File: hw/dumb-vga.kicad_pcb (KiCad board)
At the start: 2 copper layers, 62.2 x 83.8 mm, 26 parts, among them IC1 74HC590N, IC2 74HC590N, IC3 74HC590N, IC4 74HC574N, P1 CONN_01X02, P2 CONN_01X03, P3 CONN_01X03, U1 A29040C, X1 VGAF

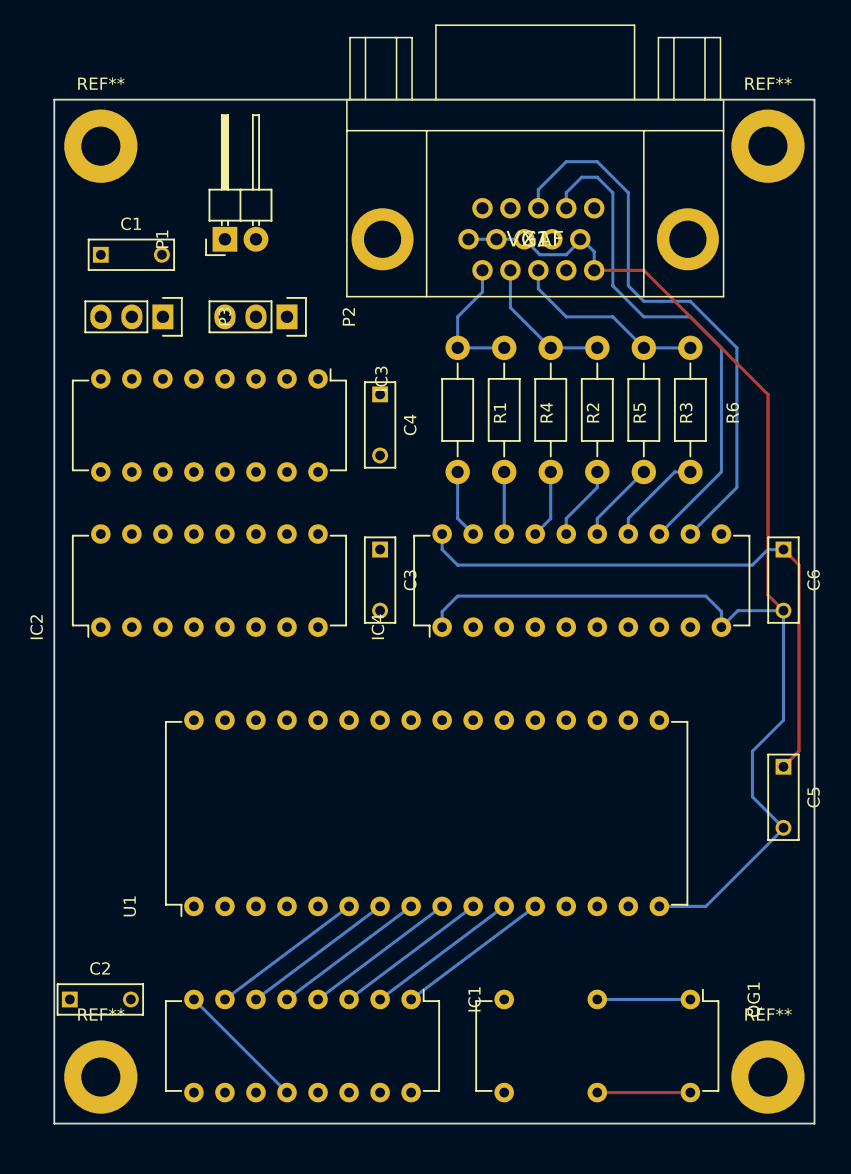
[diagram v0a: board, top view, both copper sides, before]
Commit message: Rearranged memory lines to make PCB layout easier, laid out more PCB.
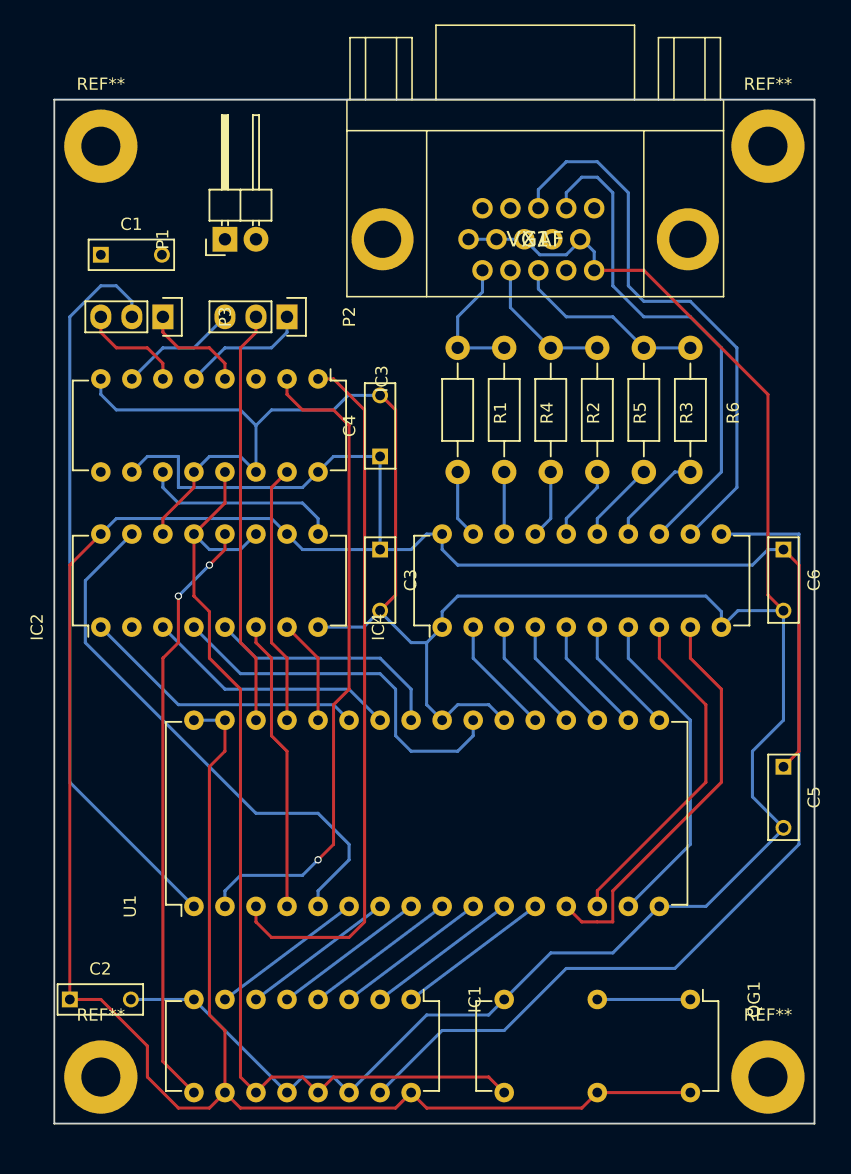
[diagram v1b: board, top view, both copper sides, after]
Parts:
- moved C4 5.08 mm to (130.8, 62.2), turned to 90 degrees
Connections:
- U1 pad 13: Net-(IC4-Pad2) -> Net-(IC4-Pad9)
- U1 pad 14: Net-(IC4-Pad3) -> Net-(IC4-Pad8)
- U1 pad 15: Net-(IC4-Pad4) -> Net-(IC4-Pad7)
- U1 pad 17: Net-(IC4-Pad5) -> Net-(IC4-Pad6)
- U1 pad 18: Net-(IC4-Pad6) -> Net-(IC4-Pad5)
- U1 pad 19: Net-(IC4-Pad7) -> Net-(IC4-Pad4)
- U1 pad 20: Net-(IC4-Pad8) -> Net-(IC4-Pad3)
- U1 pad 21: Net-(IC4-Pad9) -> Net-(IC4-Pad2)
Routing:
- net VCC: track 56.7 -> 243.0 mm
- net GND: track 125.6 -> 255.0 mm
- net Net-(IC1-Pad11): track 0.00 -> 82.5 mm
- net Net-(IC1-Pad15): track 0.00 -> 74.5 mm
- net Net-(P3-Pad2): track 0.00 -> 60.4 mm
- net Net-(IC3-Pad1): track 0.00 -> 58.0 mm
- net Net-(IC3-Pad2): track 0.00 -> 54.0 mm, vias 0 -> 1
- net Net-(IC1-Pad9): track 0.00 -> 48.9 mm, vias 0 -> 2
- net Net-(IC2-Pad15): track 0.00 -> 45.0 mm
- net Net-(P2-Pad2): track 0.00 -> 34.1 mm
- net Net-(IC4-Pad9): track 0.00 -> 33.2 mm
- net Net-(IC2-Pad4): track 0.00 -> 31.1 mm
- net Net-(IC4-Pad8): track 0.00 -> 28.1 mm
- net Net-(IC4-Pad7): track 0.00 -> 27.1 mm
- net Net-(IC2-Pad6): track 0.00 -> 23.9 mm
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
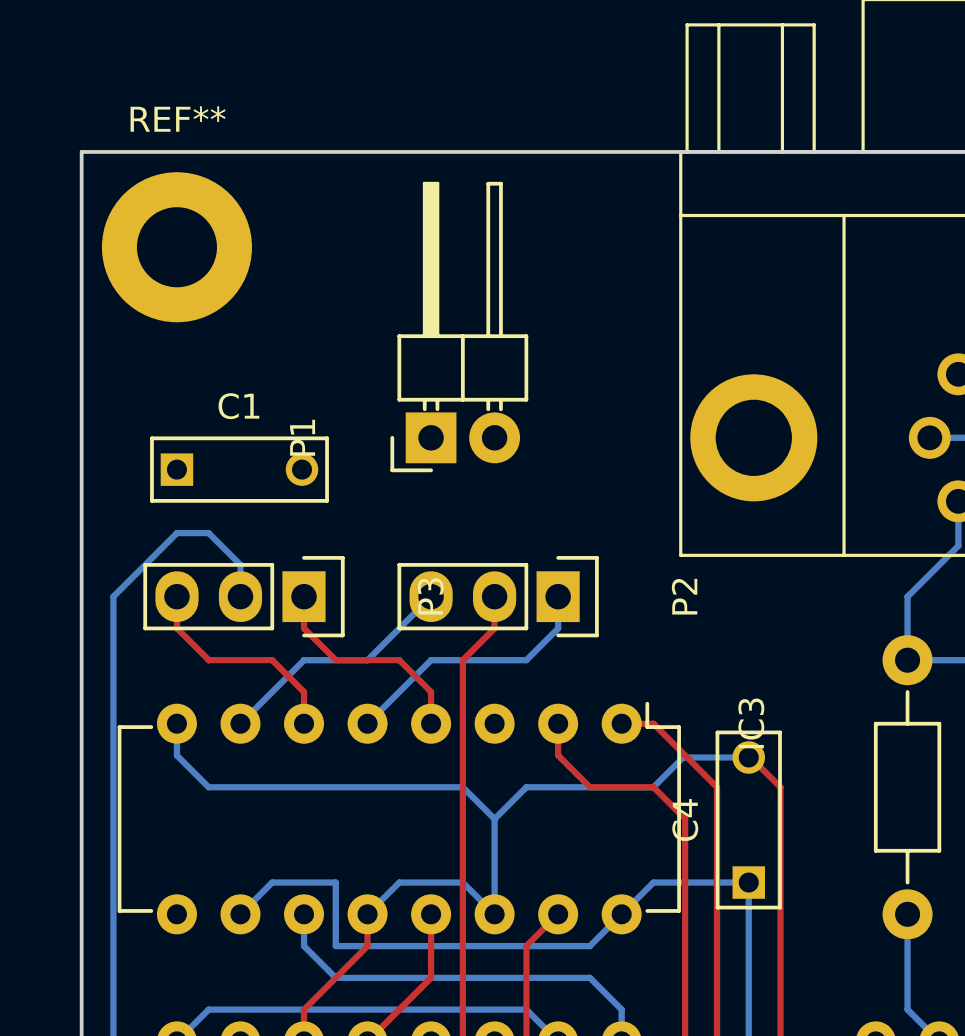
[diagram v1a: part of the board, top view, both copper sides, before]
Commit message: Changed power connector for something I have
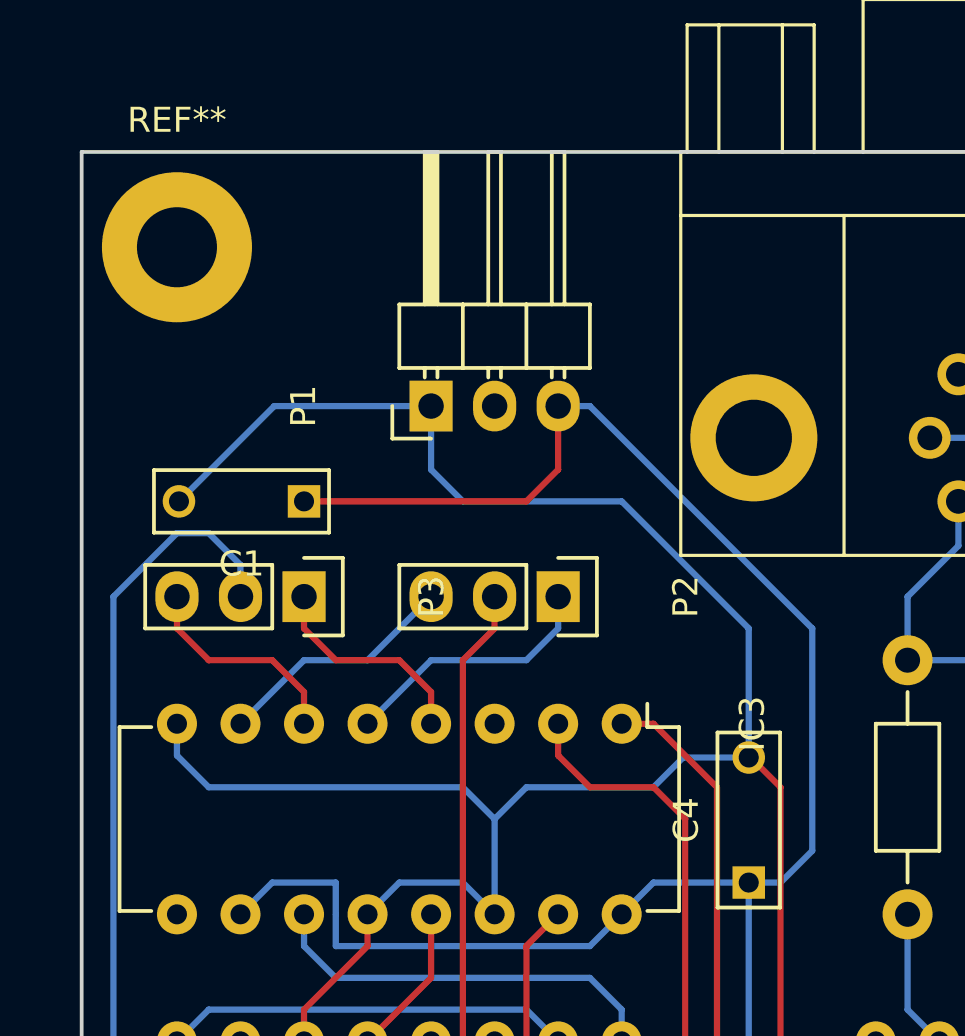
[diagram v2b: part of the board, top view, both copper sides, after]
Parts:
- P1: value CONN_01X02 -> CONN_01X03; footprint Pin_Headers:Pin_Header_Angled_1x02 -> Pin_Headers:Pin_Header_Angled_1x03
- moved C1 5.24 mm to (113.0, 47.0), turned to 180 degrees
- moved P1 1.27 mm to (118.1, 43.2)
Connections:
- P1 pad 2: VCC -> (no net)
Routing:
- net VCC: track 243.0 -> 282.0 mm
- net GND: track 255.0 -> 289.7 mm

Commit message: PCB tidy-up
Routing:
- added copper zone on B.Cu, net GND
- added copper zone on F.Cu, net GND
- added copper zone on F.Cu, net VCC
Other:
- net class Power added: clearance 0.2, trace_width 0.6, via_dia 0.6, via_drill 0.4

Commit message: Bumping schematic version number, labelling up PCB
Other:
- board text added: "dumb_vga - 2016 - v0.7"
- board text added: "sgf@arbitrary.name"
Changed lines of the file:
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@@
     (links 96)
     (no_connects 0)
-    (area 104.064999 32.944999 166.445001 116.915001)
+    (area 96.135475 26.663039 176.914525 119.085)
     (thickness 1.6)
-    (drawings 4)
+    (drawings 6)
     (tracks 333)
     (zones 0)
@@
   )
   (page A4)
+  (title_block
+    (title "Dumb VGA")
+    (rev v0.7)
+    (comment 1 "Simple circuit to generate VGA-like signal")
+  )
   (layers
-    (0 F.Cu signal hide)
+    (0 F.Cu signal)
     (31 B.Cu signal)
     (32 B.Adhes user)
@@
     (descr "14-lead dip package, row spacing 7.62 mm (300 mils)")
     (tags "dil dip 2.54 300")
-    (fp_text reference QG1 (at 0 -5.22 270) (layer F.SilkS)
+    (fp_text reference QG1 (at 3.81 7.62 360) (layer F.SilkS)
       (effects (font (size 1 1) (thickness 0.15)))
     )
@@
   (module Wire_Pads:SolderWirePad_single_2-5mmDrill (layer F.Cu)
     (at 162.56 113.03)
-    (fp_text reference REF** (at 0 -5.08) (layer F.SilkS)
+    (fp_text reference REF** (at 0 -5.08) (layer F.SilkS) hide
       (effects (font (size 1 1) (thickness 0.15)))
     )
@@
   (module Wire_Pads:SolderWirePad_single_2-5mmDrill (layer F.Cu)
     (at 107.95 113.03)
-    (fp_text reference REF** (at 0 -5.08) (layer F.SilkS)
+    (fp_text reference REF** (at 0 -5.08) (layer F.SilkS) hide
       (effects (font (size 1 1) (thickness 0.15)))
     )
@@
   (module Wire_Pads:SolderWirePad_single_2-5mmDrill (layer F.Cu)
     (at 107.95 36.83)
-    (fp_text reference REF** (at 0 -5.08) (layer F.SilkS)
+    (fp_text reference REF** (at 0 -5.08) (layer F.SilkS) hide
       (effects (font (size 1 1) (thickness 0.15)))
     )
@@
     (at 143.51 44.45)
     (attr virtual)
-    (fp_text reference X1 (at 0 0) (layer F.SilkS)
+    (fp_text reference X1 (at 0 0) (layer F.SilkS) hide
       (effects (font (thickness 0.15)))
     )
-    (fp_text value VGAF (at 0 0) (layer F.SilkS)
+    (fp_text value VGAF (at 0 0) (layer F.SilkS) hide
       (effects (font (thickness 0.15)))
     )
@@
     (descr "Film Capacitor Length 7mm x Width 2.5mm, Pitch 5mm")
     (tags Capacitor)
-    (fp_text reference C1 (at 2.5 -2.5 180) (layer F.SilkS)
+    (fp_text reference C1 (at 2.5 0 180) (layer F.SilkS)
       (effects (font (size 1 1) (thickness 0.15)))
     )
@@
     (descr "16-lead dip package, row spacing 7.62 mm (300 mils)")
     (tags "dil dip 2.54 300")
-    (fp_text reference IC1 (at 0 -5.22 270) (layer F.SilkS)
+    (fp_text reference IC1 (at 3.81 8.89 360) (layer F.SilkS)
       (effects (font (size 1 1) (thickness 0.15)))
     )
@@
     (descr "16-lead dip package, row spacing 7.62 mm (300 mils)")
     (tags "dil dip 2.54 300")
-    (fp_text reference IC2 (at 0 -5.22 90) (layer F.SilkS)
+    (fp_text reference IC2 (at 3.81 8.89 180) (layer F.SilkS)
       (effects (font (size 1 1) (thickness 0.15)))
     )
@@
     (descr "16-lead dip package, row spacing 7.62 mm (300 mils)")
     (tags "dil dip 2.54 300")
-    (fp_text reference IC3 (at 0 -5.22 270) (layer F.SilkS)
+    (fp_text reference IC3 (at 3.81 8.89 360) (layer F.SilkS)
       (effects (font (size 1 1) (thickness 0.15)))
     )
@@
     (descr "20-lead dip package, row spacing 7.62 mm (300 mils)")
     (tags "dil dip 2.54 300")
-    (fp_text reference IC4 (at 0 -5.22 90) (layer F.SilkS)
+    (fp_text reference IC4 (at 3.81 11.43 180) (layer F.SilkS)
       (effects (font (size 1 1) (thickness 0.15)))
     )
@@
     (descr "Resistor, Axial,  RM 10mm, 1/3W,")
     (tags "Resistor, Axial, RM 10mm, 1/3W,")
-    (fp_text reference R1 (at 0.24892 -3.50012 270) (layer F.SilkS)
+    (fp_text reference R1 (at 0.24892 0 270) (layer F.SilkS)
       (effects (font (size 1 1) (thickness 0.15)))
     )
@@
     (descr "Resistor, Axial,  RM 10mm, 1/3W,")
     (tags "Resistor, Axial, RM 10mm, 1/3W,")
-    (fp_text reference R2 (at 0.24892 -3.50012 270) (layer F.SilkS)
+    (fp_text reference R2 (at 0.24892 0 270) (layer F.SilkS)
       (effects (font (size 1 1) (thickness 0.15)))
     )
@@
     (descr "Resistor, Axial,  RM 10mm, 1/3W,")
     (tags "Resistor, Axial, RM 10mm, 1/3W,")
-    (fp_text reference R3 (at 0.24892 -3.50012 270) (layer F.SilkS)
+    (fp_text reference R3 (at 0.24892 0 270) (layer F.SilkS)
       (effects (font (size 1 1) (thickness 0.15)))
     )
@@
     (descr "Resistor, Axial,  RM 10mm, 1/3W,")
     (tags "Resistor, Axial, RM 10mm, 1/3W,")
-    (fp_text reference R4 (at 0.24892 -3.50012 270) (layer F.SilkS)
+    (fp_text reference R4 (at 0.24892 0 270) (layer F.SilkS)
       (effects (font (size 1 1) (thickness 0.15)))
     )
@@
     (descr "Resistor, Axial,  RM 10mm, 1/3W,")
     (tags "Resistor, Axial, RM 10mm, 1/3W,")
-    (fp_text reference R5 (at 0.24892 -3.50012 270) (layer F.SilkS)
+    (fp_text reference R5 (at 0.24892 0 270) (layer F.SilkS)
       (effects (font (size 1 1) (thickness 0.15)))
     )
@@
     (descr "Resistor, Axial,  RM 10mm, 1/3W,")
     (tags "Resistor, Axial, RM 10mm, 1/3W,")
-    (fp_text reference R6 (at 0.24892 -3.50012 270) (layer F.SilkS)
+    (fp_text reference R6 (at 0.24892 0 270) (layer F.SilkS)
       (effects (font (size 1 1) (thickness 0.15)))
     )
@@
     (descr "32-lead dip package, row spacing 15.24 mm (600 mils)")
     (tags "dil dip 2.54 600")
-    (fp_text reference U1 (at 0 -5.22 90) (layer F.SilkS)
+    (fp_text reference U1 (at 7.62 19.05 180) (layer F.SilkS)
       (effects (font (size 1 1) (thickness 0.15)))
     )
@@
     (descr "Film Capacitor Length 7mm x Width 2.5mm, Pitch 5mm")
     (tags Capacitor)
-    (fp_text reference C2 (at 2.5 -2.5) (layer F.SilkS)
+    (fp_text reference C2 (at 2.54 0) (layer F.SilkS)
       (effects (font (size 1 1) (thickness 0.15)))
     )
@@
     (descr "Film Capacitor Length 7mm x Width 2.5mm, Pitch 5mm")
     (tags Capacitor)
-    (fp_text reference C3 (at 2.5 -2.5 270) (layer F.SilkS)
+    (fp_text reference C3 (at 2.5 0 270) (layer F.SilkS)
       (effects (font (size 1 1) (thickness 0.15)))
     )
@@
     (descr "Film Capacitor Length 7mm x Width 2.5mm, Pitch 5mm")
     (tags Capacitor)
-    (fp_text reference C4 (at 2.5 -2.5 90) (layer F.SilkS)
+    (fp_text reference C4 (at 2.5 0 90) (layer F.SilkS)
       (effects (font (size 1 1) (thickness 0.15)))
     )
@@
     (descr "Film Capacitor Length 7mm x Width 2.5mm, Pitch 5mm")
     (tags Capacitor)
-    (fp_text reference C5 (at 2.5 -2.5 270) (layer F.SilkS)
+    (fp_text reference C5 (at 2.54 0 270) (layer F.SilkS)
       (effects (font (size 1 1) (thickness 0.15)))
     )
@@
     (descr "Film Capacitor Length 7mm x Width 2.5mm, Pitch 5mm")
     (tags Capacitor)
-    (fp_text reference C6 (at 2.5 -2.5 270) (layer F.SilkS)
+    (fp_text reference C6 (at 2.5 0 270) (layer F.SilkS)
       (effects (font (size 1 1) (thickness 0.15)))
     )
@@
     (descr "Through hole pin header")
     (tags "pin header")
-    (fp_text reference P2 (at 0 -5.1 270) (layer F.SilkS)
+    (fp_text reference P2 (at 2.54 2.54 360) (layer F.SilkS)
       (effects (font (size 1 1) (thickness 0.15)))
     )
@@
     (descr "Through hole pin header")
     (tags "pin header")
-    (fp_text reference P3 (at 0 -5.1 270) (layer F.SilkS)
+    (fp_text reference P3 (at 2.54 2.54 360) (layer F.SilkS)
       (effects (font (size 1 1) (thickness 0.15)))
     )
@@
   (module Wire_Pads:SolderWirePad_single_2-5mmDrill (layer F.Cu)
     (at 162.56 36.83)
-    (fp_text reference REF** (at 0 -5.08) (layer F.SilkS)
+    (fp_text reference REF** (at 0 -5.08) (layer F.SilkS) hide
       (effects (font (size 1 1) (thickness 0.15)))
     )
@@
     (descr "Through hole pin header")
     (tags "pin header")
-    (fp_text reference P1 (at 0 -5.1 90) (layer F.SilkS)
+    (fp_text reference P1 (at 0 -2.54 90) (layer F.SilkS)
       (effects (font (size 1 1) (thickness 0.15)))
     )
@@
     )
   )
+  (gr_text "dumb_vga - 2016 - v0.7" (at 163.83 64.77 90) (layer F.SilkS)
+    (effects (font (size 1 1) (thickness 0.15)) (justify left))
+  )
+  (gr_text sgf@arbitrary.name (at 161.29 64.77 90) (layer F.SilkS)
+    (effects (font (size 1 1) (thickness 0.15)) (justify left))
+  )
   (gr_line (start 104.14 116.84) (end 104.14 33.02) (angle 90) (layer Edge.Cuts) (width 0.15))

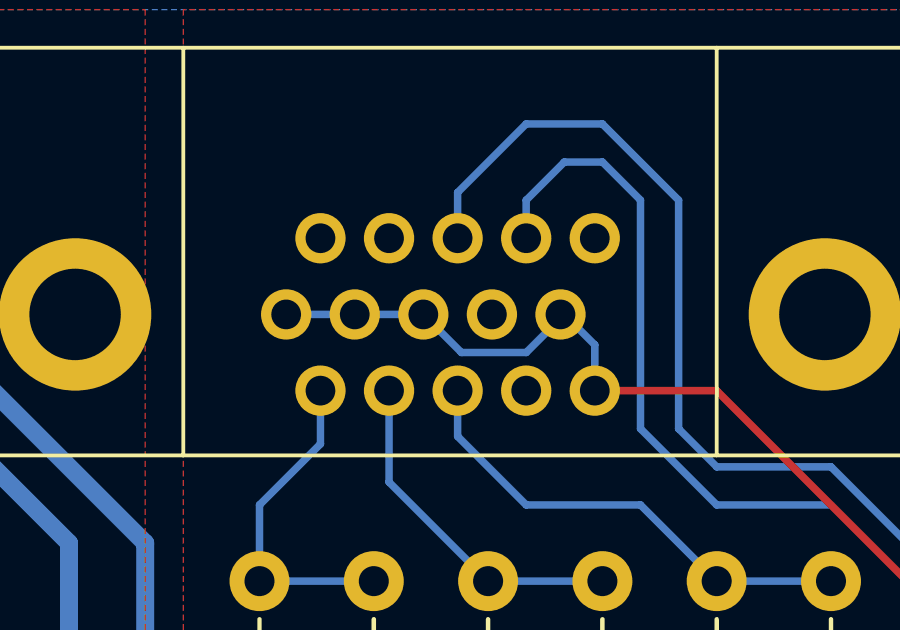
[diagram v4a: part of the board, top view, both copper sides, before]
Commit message: Switched to VGA connector with soldermask on the bottom
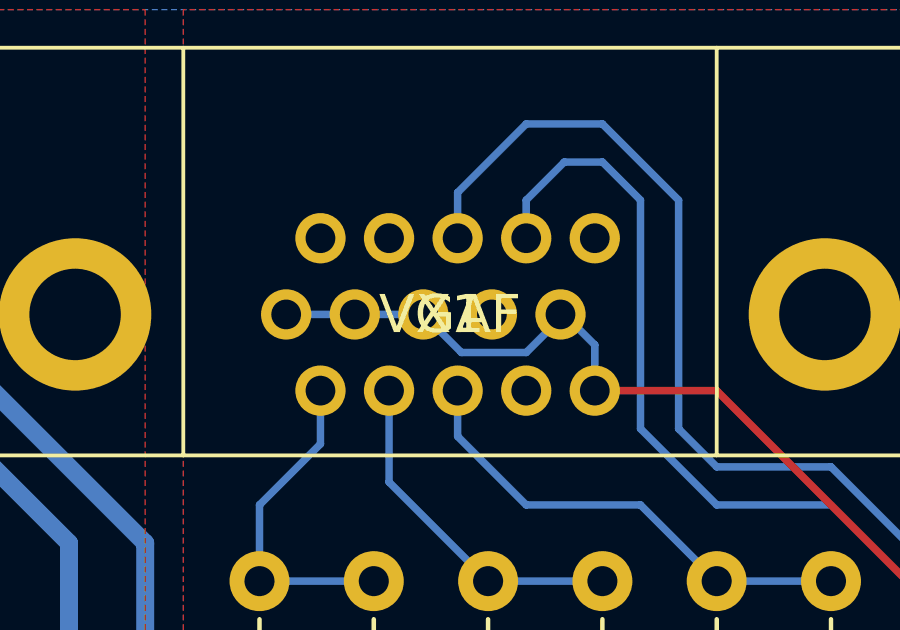
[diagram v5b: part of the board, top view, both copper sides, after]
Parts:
- X1: footprint HD15_B:HD15_B-HD15F -> hw:hd15f
